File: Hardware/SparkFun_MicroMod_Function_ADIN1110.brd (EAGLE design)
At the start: 38 x 65 mm, 125 parts, among them J1 IP20(RJ50), J2 MICROMOD_FUNCTION_STANDARD, Q1 220mA/50V/3.5Ω, Q2 20V/4.2A/52mΩ/1.4W, T1 WE-STST, U1 ADIN1110, U2 EEPROM, U3 3.3V, U4 WE-TVS, Y1 25MHz

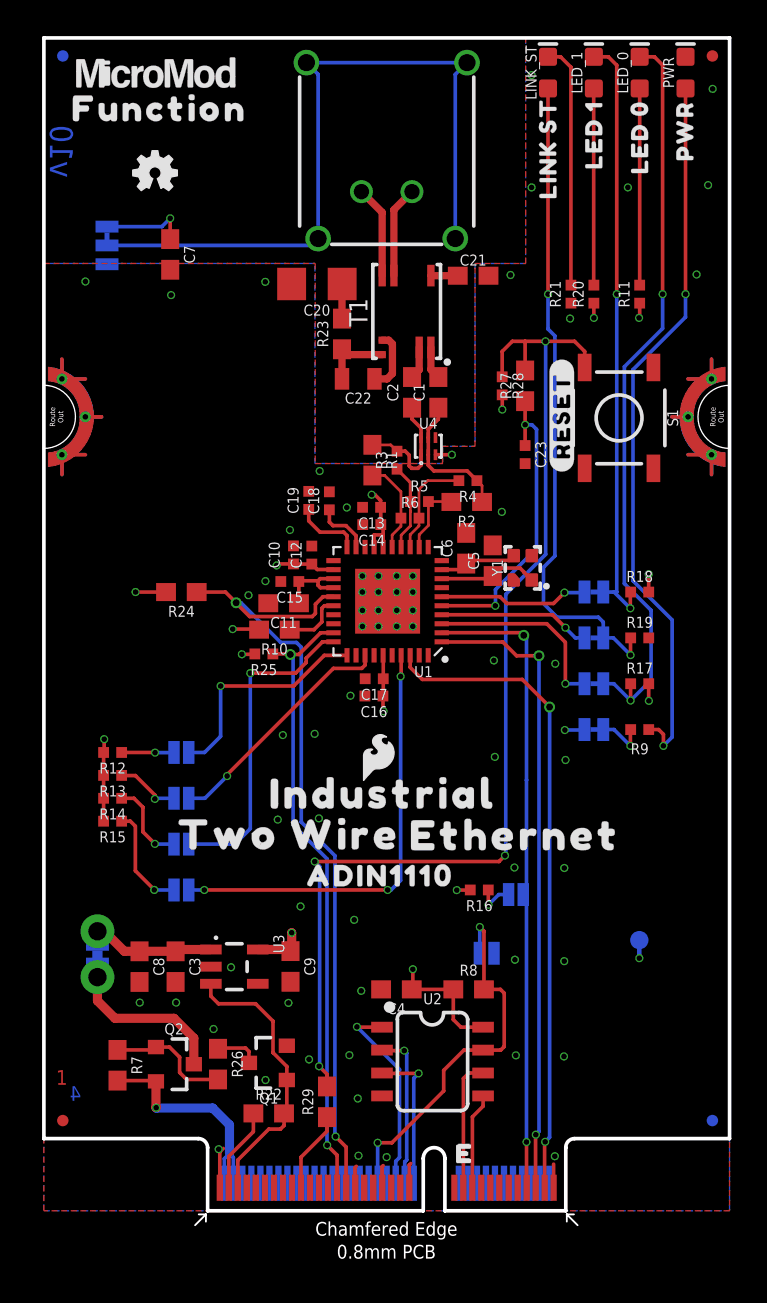
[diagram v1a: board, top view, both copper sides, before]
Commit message: Silk updated to "Single Pair Ethernet"
-updated product name silk
-bumped version to v11 in brd and sch
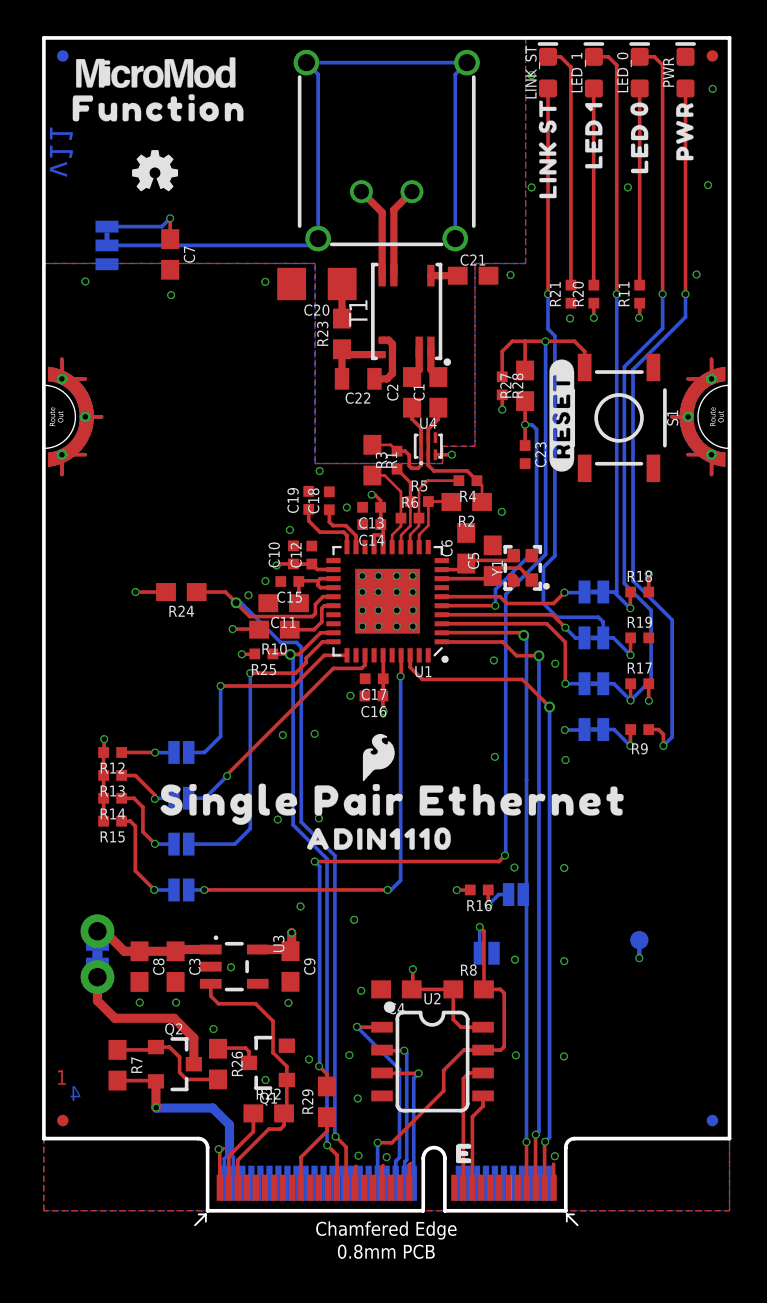
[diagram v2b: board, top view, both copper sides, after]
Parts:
- removed U$19, U$2: (no value), output:INDUSTRIAL0
- removed U$20, U$3: (no value), output:ETHERNET0
- removed U$30, U$32: (no value), output:TWO_WIRE3
- added U$17, U$18: (no value), output:SINGLE_PAIR_ETHERNET0
- moved U$4 2.03 mm to (18.7, 20.6)
- moved U$21 1.80 mm to (19.8, 38.3)
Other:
- board text added: "v11"
- board text removed: "v10"
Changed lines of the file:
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@@
 <drawing>
 <settings>
-<setting alwaysvectorfont="no"/>
+<setting alwaysvectorfont="yes"/>
 <setting verticaltext="up"/>
 </settings>
@@
 <layer number="98" name="Guide" color="6" fill="1" visible="no" active="no"/>
 <layer number="99" name="SpiceOrder" color="7" fill="1" visible="no" active="no"/>
-<layer number="100" name="Muster" color="7" fill="1" visible="yes" active="yes"/>
+<layer number="100" name="Muster" color="7" fill="1" visible="no" active="yes"/>
 <layer number="101" name="Patch_Top" color="12" fill="4" visible="no" active="no"/>
 <layer number="102" name="Vscore" color="7" fill="1" visible="no" active="no"/>
@@
 <plain>
 <wire x1="28.925" y1="0" x2="22.225" y2="0" width="0.2032" layer="20"/>
-<text x="0.9686" y="58.713278125" size="1.27" layer="16" font="vector" ratio="20" rot="SMR90" align="center">v10</text>
+<text x="0.9686" y="58.713278125" size="1.27" layer="16" font="vector" ratio="20" rot="SMR90" align="center">v11</text>
 <text x="19.95" y="-14.77" size="1.778" layer="51" font="vector" ratio="10">Pete Lewis</text>
 <wire x1="21.025" y1="0" x2="9.075" y2="0" width="0.2032" layer="20"/>
@@
 <attribute name="VALUE" x="22.471378125" y="45.3009" size="0.6096" layer="27" font="vector" ratio="20" rot="R90" align="top-center"/>
 </element>
-<element name="U$2" library="output" package="INDUSTRIAL0" value="" x="18.796" y="23.114" smashed="yes"/>
-<element name="U$3" library="output" package="ETHERNET0" value="" x="26.106" y="20.808" smashed="yes"/>
-<element name="U$4" library="output" package="ADIN11100" value="" x="18.662" y="18.566" smashed="yes"/>
+<element name="U$4" library="output" package="ADIN11100" value="" x="18.662" y="20.598" smashed="yes"/>
 <element name="U$5" library="SparkFun-Aesthetics" package="SFE_LOGO_FLAME_.1" value="" x="18.542" y="25.146" smashed="yes"/>
 <element name="U$1" library="output" package="#RESET#0" value="" x="28.702" y="44.069" smashed="yes" rot="R90"/>
@@
 <element name="U$15" library="output" package="#MS_SEL#2" value="" x="11.684" y="20.32" smashed="yes" rot="MR0"/>
 <element name="U$16" library="output" package="#SPI_CFG0#0" value="" x="30.861" y="17.526" smashed="yes" rot="MR0"/>
-<element name="U$19" library="output" package="INDUSTRIAL0" value="" x="19.431" y="42.418" smashed="yes" rot="MR0"/>
-<element name="U$20" library="output" package="ETHERNET0" value="" x="19.361" y="38.442" smashed="yes" rot="MR0"/>
-<element name="U$21" library="output" package="ADIN11100" value="" x="19.555" y="36.48" smashed="yes" rot="MR0"/>
+<element name="U$21" library="output" package="ADIN11100" value="" x="19.809" y="38.258" smashed="yes" rot="MR0"/>
 <element name="U$24" library="output" package="FUNCTION0" value="" x="6.167" y="61.088" smashed="yes" rot="MR0"/>
 <element name="U$23" library="output" package="LED_03" value="" x="33.020040625" y="59.5204" smashed="yes" rot="R90"/>
@@
 <element name="U$29" library="output" package="#LED1#21" value="" x="33.71" y="34.31" smashed="yes" rot="MR0"/>
 <element name="U$31" library="ADIN1110" package="#LINKST#2" value="" x="34.35" y="31.74" smashed="yes" rot="MR0"/>
-<element name="U$30" library="output" package="TWO_WIRE3" value="" x="19.33" y="40.36" smashed="yes" rot="MR0"/>
-<element name="U$32" library="output" package="TWO_WIRE3" value="" x="13.6" y="20.85" smashed="yes"/>
 <element name="R24" library="SparkFun-Resistors" package="0603" value="1.5k" x="7.62" y="34.29" smashed="yes" rot="R180">
 <attribute name="NAME" x="7.62" y="33.528" size="0.6096" layer="25" font="vector" ratio="20" rot="R180" align="bottom-center"/>
@@
 <element name="CS" library="SparkFun-Connectors" package="TP_15TH" value="" x="13.657578125" y="30.83051875" smashed="yes"/>
 <element name="INT" library="SparkFun-Connectors" package="TP_15TH" value="" x="10.6553" y="33.698178125" smashed="yes"/>
+<element name="U$17" library="output" package="SINGLE_PAIR_ETHERNET0" value="" x="19.431" y="22.733" smashed="yes"/>
+<element name="U$18" library="output" package="SINGLE_PAIR_ETHERNET0" value="" x="19.304" y="41.021" smashed="yes" rot="MR0"/>
 </elements>
 <signals>

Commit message: reduced width by 0.01" on each side
-This will help avoid overlap issues when plugging in two of these boards into the main-double.
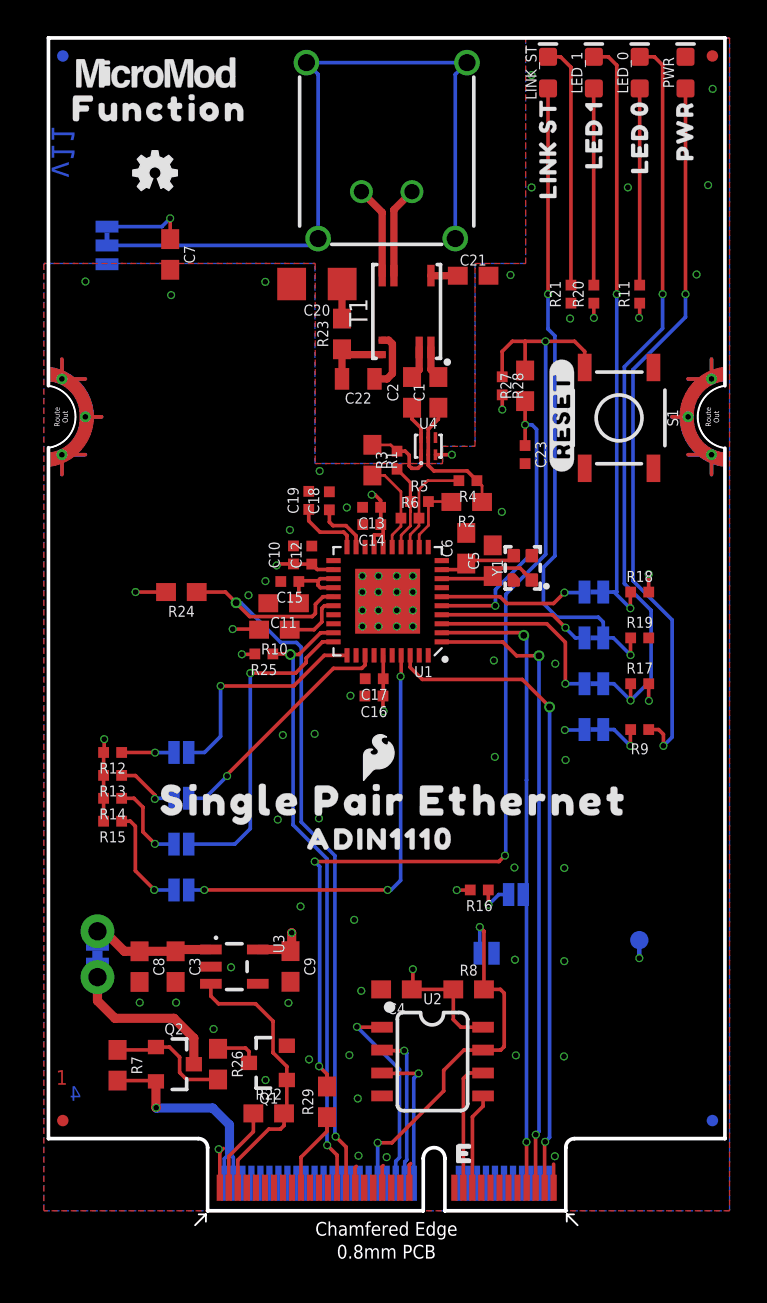
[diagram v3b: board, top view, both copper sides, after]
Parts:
- moved U$31 0.19 mm to (34.2, 31.8)
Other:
- board size 38 x 65 mm -> 37.5 x 65 mm
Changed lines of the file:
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@@
 <drawing>
 <settings>
-<setting alwaysvectorfont="yes"/>
+<setting alwaysvectorfont="no"/>
 <setting verticaltext="up"/>
 </settings>
-<grid distance="0.05" unitdist="inch" unit="inch" style="lines" multiple="1" display="yes" altdistance="0.005" altunitdist="inch" altunit="inch"/>
+<grid distance="0.001" unitdist="inch" unit="inch" style="lines" multiple="1" display="yes" altdistance="0.0001" altunitdist="inch" altunit="inch"/>
 <layers>
 <layer number="1" name="Top/Horz" color="4" fill="1" visible="yes" active="yes"/>
@@
 <plain>
 <wire x1="28.925" y1="0" x2="22.225" y2="0" width="0.2032" layer="20"/>
-<text x="0.9686" y="58.713278125" size="1.27" layer="16" font="vector" ratio="20" rot="SMR90" align="center">v11</text>
+<text x="1.06511875" y="58.700578125" size="1.27" layer="16" font="vector" ratio="20" rot="SMR90" align="center">v11</text>
 <text x="19.95" y="-14.77" size="1.778" layer="51" font="vector" ratio="10">Pete Lewis</text>
 <wire x1="21.025" y1="0" x2="9.075" y2="0" width="0.2032" layer="20"/>
 <wire x1="28.925" y1="0" x2="28.925" y2="3.5" width="0.2032" layer="20"/>
 <wire x1="28.925" y1="3.5" x2="29.4" y2="4" width="0.2032" layer="20" curve="-90"/>
-<wire x1="29.4" y1="4" x2="38" y2="4" width="0.2032" layer="20"/>
-<wire x1="38" y1="4" x2="38" y2="65" width="0.2032" layer="20"/>
-<wire x1="38" y1="65" x2="0" y2="65" width="0.2032" layer="20"/>
-<wire x1="0" y1="65" x2="0" y2="4" width="0.2032" layer="20"/>
+<wire x1="29.4" y1="4" x2="37.7444" y2="4" width="0.2032" layer="20"/>
+<wire x1="37.7444" y1="4" x2="37.7444" y2="42.2656" width="0.2032" layer="20"/>
+<wire x1="37.7444" y1="45.72" x2="37.7444" y2="65" width="0.2032" layer="20"/>
+<wire x1="37.7444" y1="65" x2="0.254" y2="65" width="0.2032" layer="20"/>
+<wire x1="0.254" y1="65" x2="0.254" y2="45.72" width="0.2032" layer="20"/>
+<wire x1="0.254" y1="42.291" x2="0.254" y2="4" width="0.2032" layer="20"/>
 <wire x1="9.075" y1="0" x2="9.075" y2="3.5" width="0.2032" layer="20"/>
 <wire x1="9.075" y1="3.5" x2="8.55" y2="4" width="0.2032" layer="20" curve="90"/>
-<wire x1="8.55" y1="4" x2="0" y2="4" width="0.2032" layer="20"/>
+<wire x1="8.55" y1="4" x2="0.254" y2="4" width="0.2032" layer="20"/>
 <wire x1="22.225" y1="0" x2="22.225" y2="2.9" width="0.2032" layer="20"/>
 <wire x1="21.025" y1="0" x2="21.025" y2="2.9" width="0.2032" layer="20"/>
@@
 <dimension x1="0" y1="0" x2="0" y2="4" x3="-2.9972" y3="2" textsize="1.778" textratio="15" layer="47" dtype="vertical" unit="inch"/>
 <dimension x1="14.4018" y1="68.7324" x2="23.5966" y2="68.7324" x3="18.9992" y3="79.1972" textsize="1.778" textratio="15" layer="100" dtype="horizontal" unit="inch"/>
+<wire x1="0.254" y1="45.72" x2="0.254" y2="42.291" width="0.1016" layer="20" curve="-165"/>
+<wire x1="37.7444" y1="45.72" x2="37.7444" y2="42.2656" width="0.1016" layer="20" curve="165"/>
 </plain>
 <attributes>
@@
 <element name="U$10" library="output" package="#LED0#20" value="" x="33.84" y="29.19" smashed="yes" rot="MR0"/>
 <element name="U$29" library="output" package="#LED1#21" value="" x="33.71" y="34.31" smashed="yes" rot="MR0"/>
-<element name="U$31" library="ADIN1110" package="#LINKST#2" value="" x="34.35" y="31.74" smashed="yes" rot="MR0"/>
+<element name="U$31" library="ADIN1110" package="#LINKST#2" value="" x="34.1620375" y="31.7527" smashed="yes" rot="MR0"/>
 <element name="R24" library="SparkFun-Resistors" package="0603" value="1.5k" x="7.62" y="34.29" smashed="yes" rot="R180">
 <attribute name="NAME" x="7.62" y="33.528" size="0.6096" layer="25" font="vector" ratio="20" rot="R180" align="bottom-center"/>

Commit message: R27 changed to 4.7K
-updated prod_id and values on boat single and panel files.
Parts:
- R27: value 10k -> 4.7k
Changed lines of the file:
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@@
 <attribute name="VALUE" x="9.9314" y="10.414" size="0.6096" layer="27" font="vector" ratio="20" rot="R270" align="top-center"/>
 </element>
-<element name="R27" library="SparkFun-Resistors" package="0603" value="10k" x="26.67" y="45.72" smashed="yes" rot="R90">
+<element name="R27" library="SparkFun-Resistors" package="0603" value="4.7k" x="26.67" y="45.72" smashed="yes" rot="R90">
 <attribute name="NAME" x="25.908" y="45.72" size="0.6096" layer="25" font="vector" ratio="20" rot="R90" align="bottom-center"/>
-<attribute name="PROD_ID" value="RES-00824" x="26.67" y="45.72" size="1.778" layer="27" font="vector" ratio="15" rot="R90" display="off"/>
-<attribute name="VALUE" x="27.432" y="45.72" size="0.6096" layer="27" font="vector" ratio="20" rot="R90" align="top-center"/>
+<attribute name="PROD_ID" value="RES-07857" x="26.67" y="45.72" size="1.778" layer="27" font="vector" ratio="15" rot="R90" display="off"/>
+<attribute name="VALUE" value="4.7k" x="27.432" y="45.72" size="0.6096" layer="27" font="vector" ratio="20" rot="R90" align="top-center"/>
 </element>
 <element name="R28" library="SparkFun-Resistors" package="0402-TIGHT" value="100k" x="25.4" y="45.72" smashed="yes" rot="R270">
